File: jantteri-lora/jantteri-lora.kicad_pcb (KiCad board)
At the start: 2 copper layers, 25.4 x 48.3 mm, 35 parts, among them J1 ANT, J2 SWD, J3 DBG, Q1 IRLML6402TRPBF, Q2 IRLML6402TRPBF, U1 lora-mod, U2 AMS1117-3.3, U3 RFM95W-868S2, U4 AP2301, U5 AP2301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

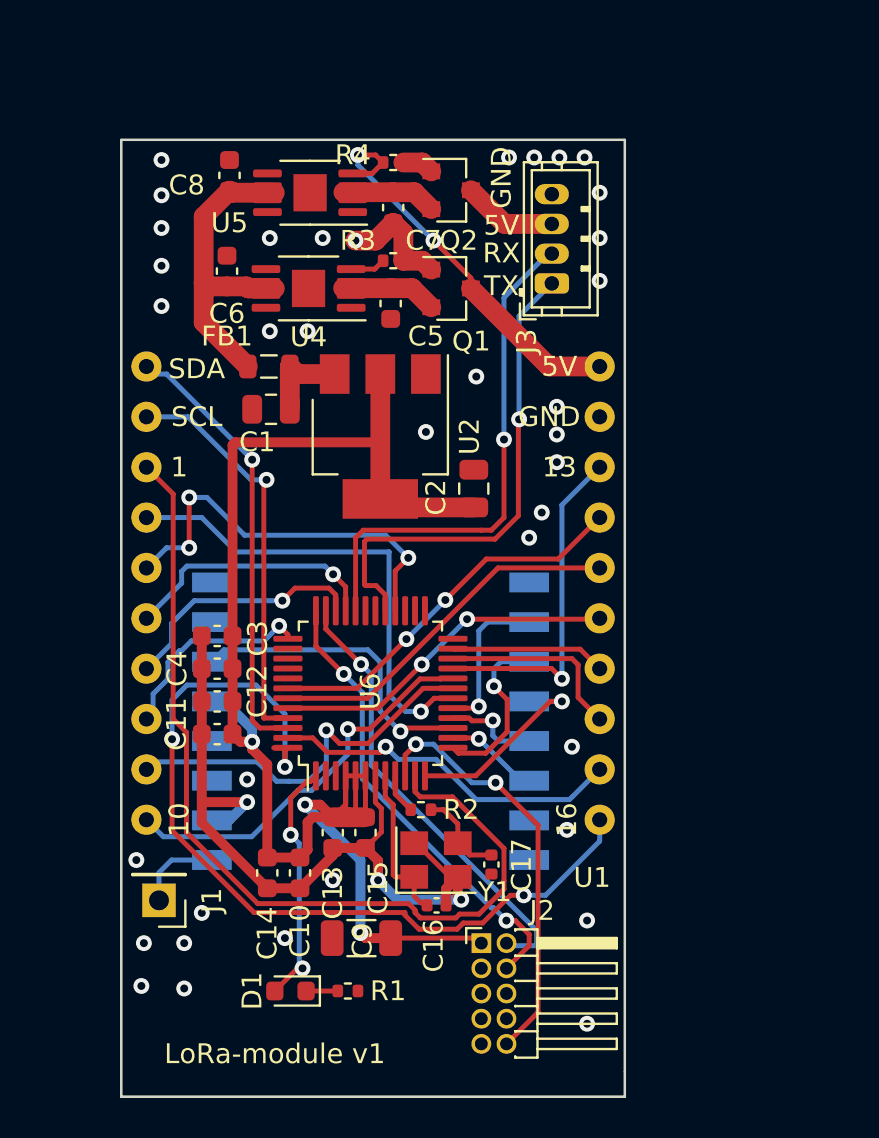
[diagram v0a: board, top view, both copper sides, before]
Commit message: Tuubijantteri design Ordered
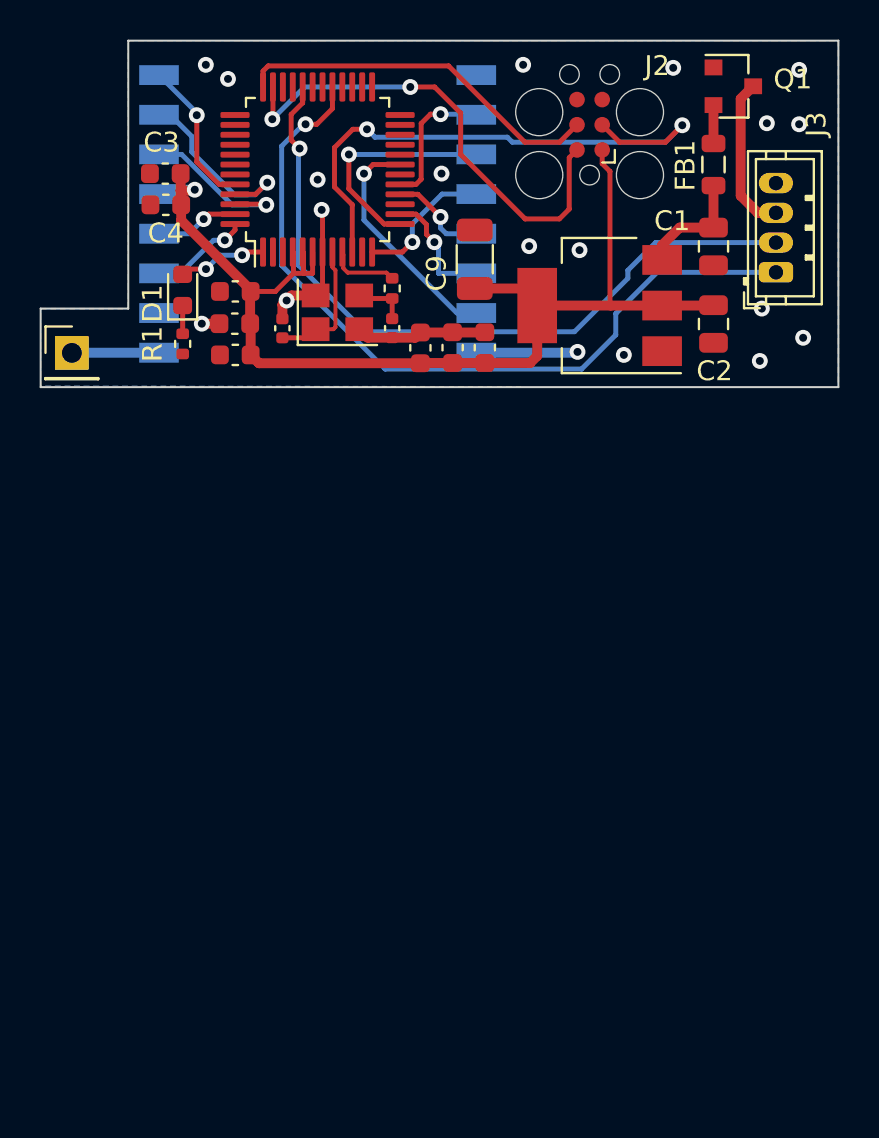
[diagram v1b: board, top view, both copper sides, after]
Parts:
- removed C5, C6, C7, C8: 100n, Capacitor_SMD:C_0603_1608Metric
- removed Q2: IRLML6402TRPBF, Package_TO_SOT_SMD:SOT-23
- removed R3, R4: 100K, Resistor_SMD:R_0402_1005Metric
- removed U1: lora-mod, voja-footprints:lora-mod
- removed U4, U5: AP2301, Package_SO:MSOP-8-1EP_3x3mm_P0.65mm_EP1.68x1.88mm
- J2: value SWD -> Conn_02x03_Odd_Even; footprint Connector_PinHeader_1.27mm:PinHeader_2x05_P1.27mm_Horizontal -> Connector:Tag-Connect_TC2030-IDC-FP_2x03_P1.27mm_Vertical
- moved J2 41.6 mm to (83.6, 44.3), turned to 90 degrees
- moved D1 35.8 mm to (63.0, 52.7), turned to 90 degrees
- moved C9 34.7 mm to (77.8, 51.1), turned to 90 degrees
- moved R1 33.7 mm to (63.0, 55.4), turned to 90 degrees
- moved C16 30.1 mm to (68.1, 54.6), turned to 90 degrees
- moved C14 29.4 mm to (65.7, 52.7), turned to 180 degrees
- moved Y1 28.1 mm to (70.8, 53.8)
- moved J1 28.0 mm to (57.5, 55.8), turned to 0 degrees
- moved C10 27.9 mm to (65.7, 54.4), turned to 180 degrees
- moved C17 27.5 mm to (73.6, 54.6)
- moved U6 26.6 mm to (69.8, 46.6)
- moved R2 26.3 mm to (73.6, 52.6), turned to 270 degrees
- moved U3 25.7 mm to (69.8, 48.8)
- moved C13 25.6 mm to (78.3, 55.6), turned to 90 degrees
- moved C15 25.0 mm to (65.7, 55.9), turned to 180 degrees
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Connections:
- net /10pinARM/SWCLK renamed /STM32G030C8T6/SWCLK
- net /10pinARM/SWDIO renamed /STM32G030C8T6/SWDIO
- net /10pinARM/SWO renamed /TC2030/SWO
- FB1 pad 2: /power_protect/OUT -> Net-(FB1-Pad2)
- J2 pad 3: GND -> /STM32G030C8T6/NRST
- Q1 pad 2: Net-(C5-Pad1) -> Net-(FB1-Pad2)
- Q1 pad 3: 5V-IN -> USB-5V
- U3 pad 11: Net-(U3-Pad11) -> RFM_DIO3
- U3 pad 12: Net-(U3-Pad12) -> RFM_DIO4
- U3 pad 15: Net-(U3-Pad15) -> RFM_DIO1
- U3 pad 16: Net-(U3-Pad16) -> RFM_DIO2
- U3 pad 7: Net-(U3-Pad7) -> RFM_DIO5
- U6 pad 10: /10pinARM/NRST -> /STM32G030C8T6/NRST
- U6 pad 11: DATA1 -> /STM32G030C8T6/PA0
- U6 pad 15: RFM_DIO0 -> /STM32G030C8T6/PA4
- U6 pad 18: DATA2 -> /STM32G030C8T6/PA7
- U6 pad 19: DATA7 -> RFM_DIO5
- U6 pad 20: DATA8 -> /STM32G030C8T6/PB1
- U6 pad 21: DATA9 -> /STM32G030C8T6/PB2
- U6 pad 22: DATA14 -> /STM32G030C8T6/PB10
- U6 pad 23: DATA13 -> /STM32G030C8T6/PB11
- U6 pad 28: DATA3 -> /STM32G030C8T6/PA8
- U6 pad 33: DATA4 -> /STM32G030C8T6/PA11
- U6 pad 34: DATA5 -> /STM32G030C8T6/PA12
- U6 pad 37: DATA6 -> /STM32G030C8T6/PA15
- U6 pad 42: DATA10 -> /STM32G030C8T6/PB3
- U6 pad 43: DATA11 -> /STM32G030C8T6/PB4
- U6 pad 44: DATA12 -> RFM_DIO2
- U6 pad 45: OUTPUT_SCL -> RFM_DIO1
- U6 pad 46: OUTPUT_SDA -> RFM_DIO0
- U6 pad 47: DATA15 -> RFM_DIO4
- U6 pad 48: DATA16 -> RFM_DIO3
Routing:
- net DATA1: track 46.3 -> 0.00 mm
- net DATA16: track 44.4 -> 0.00 mm, vias 3 -> 0
- net /STM32G030C8T6/NRST: track 0.00 -> 28.9 mm, vias 0 -> 2
- net GND: track 48.6 -> 19.7 mm, vias 40 -> 19
- net DATA2: track 25.0 -> 0.00 mm, vias 1 -> 0
- net OUTPUT_SDA: track 22.8 -> 0.00 mm, vias 1 -> 0
- net /10pinARM/NRST: track 21.4 -> 0.00 mm, vias 2 -> 0
- net OUTPUT_SCL: track 20.7 -> 0.00 mm, vias 1 -> 0
- net 5V-IN: track 20.4 -> 0.00 mm, vias 2 -> 0
- net DATA3: track 20.4 -> 0.00 mm, vias 3 -> 0
- net DATA8: track 19.9 -> 0.00 mm, vias 1 -> 0
- net DATA7: track 19.9 -> 0.00 mm, vias 1 -> 0
- net DATA10: track 19.3 -> 0.00 mm, vias 2 -> 0
- net DATA11: track 18.4 -> 0.00 mm
- net DATA15: track 17.9 -> 0.00 mm, vias 1 -> 0
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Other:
- board size 25.4 x 48.3 mm -> 40.2 x 17.5 mm
- board text removed: "1"
- board text removed: "10"
- board text removed: "13"
- board text removed: "16"
- board text removed: "5V"
- board text removed: "GND"
- board text removed: "LoRa-module v1"
- board text removed: "RX"
- board text removed: "SCL"
- board text removed: "SDA"
- board text removed: "TX"

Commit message: Update projects
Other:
- net class Default removed
